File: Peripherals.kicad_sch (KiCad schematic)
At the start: 26 parts, among them J2 Conn_01x02, M1 Vibrator DC Motor, U1 MAX30102, U10 DRV2603RUNR, U2 BMI270, U3 OPT3004DNPR, U4 LPS22DF, U5 W25Q32JVSS

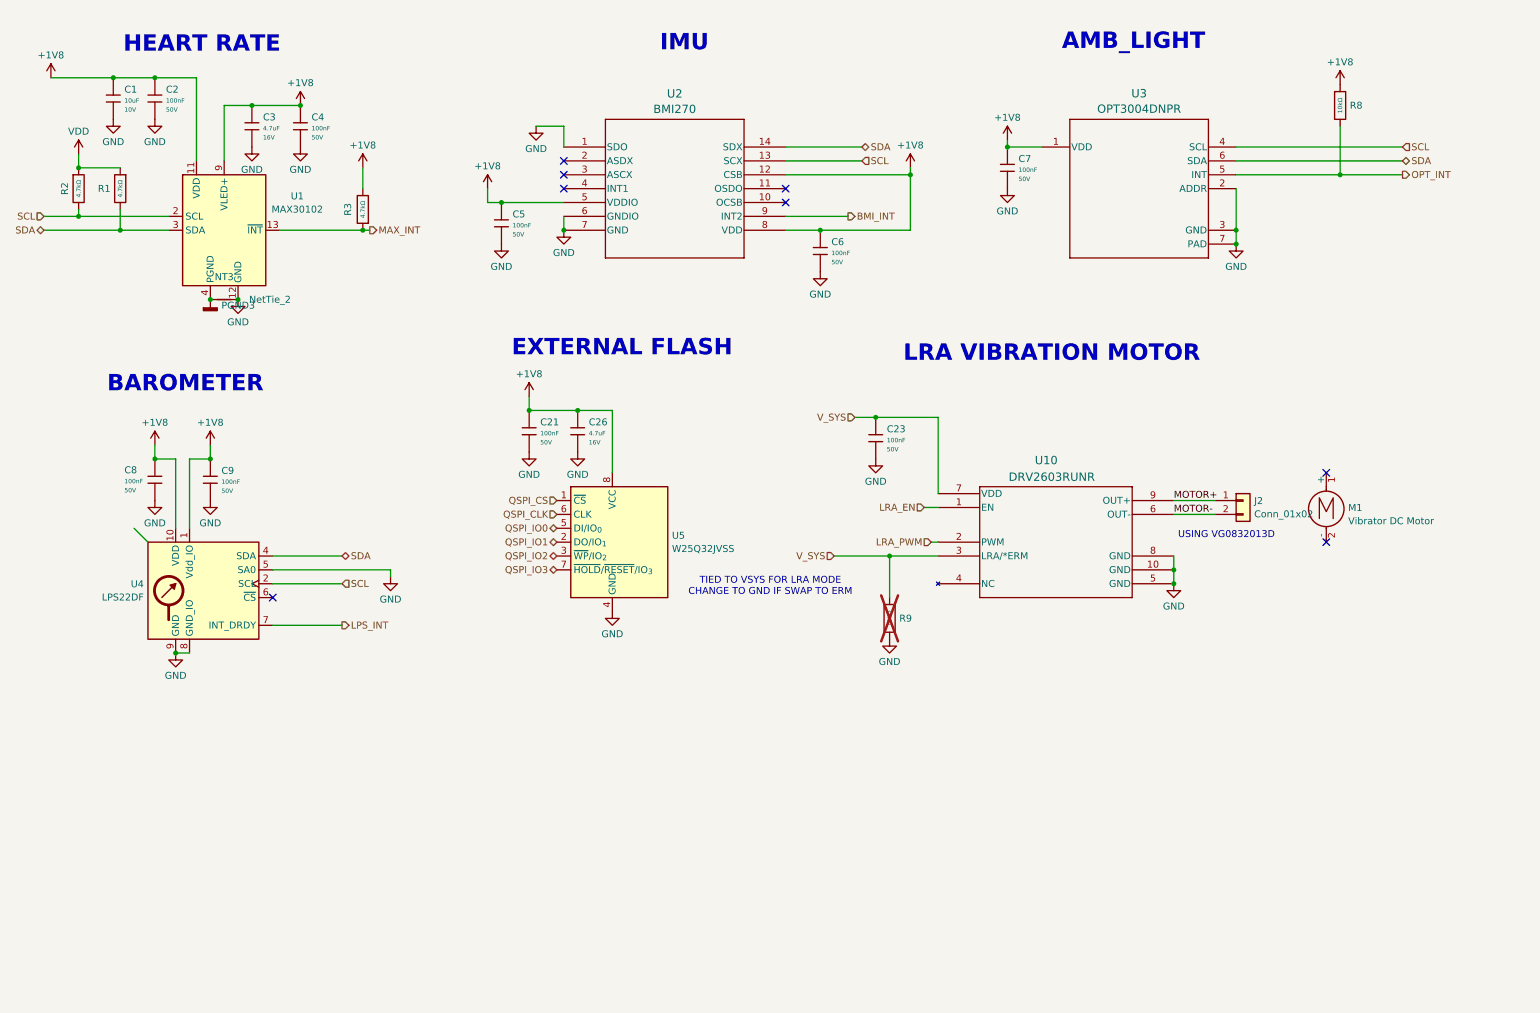
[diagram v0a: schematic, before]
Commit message: Update most sym/footprint libraries
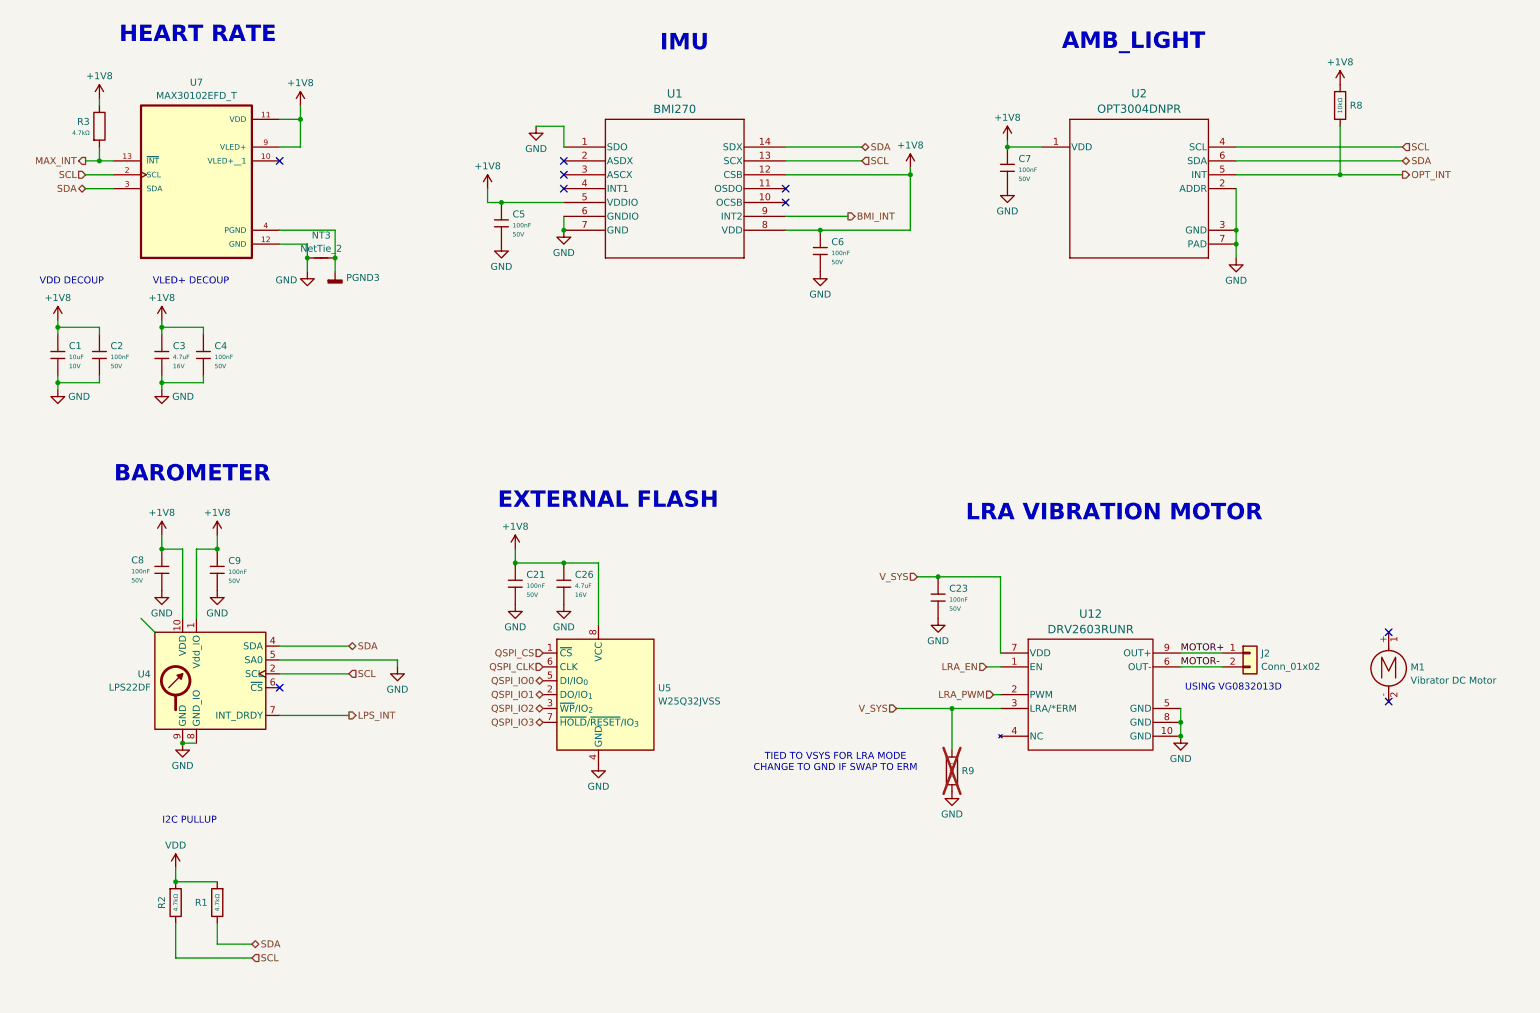
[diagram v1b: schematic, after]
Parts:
- removed U1: MAX30102, OptoDevice:Maxim_OLGA-14_3.3x5.6mm_P0.8mm, symbol Sensor:MAX30102
- removed U10: DRV2603RUNR, DRV:RUN10_TEX, symbol 2026-04-14_20-16-38:DRV2603RUNR
- removed U2: BMI270, BMI:BMI270_BOS, symbol 2026-04-08_00-20-06:BMI270
- removed U3: OPT3004DNPR, OPT:DNP0006A, symbol 2026-04-08_01-09-15:OPT3004DNPR
- added U1: BMI270, Smart_Watch:BMI270_BOS-L, symbol Smart_Watch:BMI270
- added U12: DRV2603RUNR, Smart_Watch:RUN10_TEX, symbol Smart_Watch:DRV2603RUNR
- added U2: OPT3004DNPR, Smart_Watch:DNP0006A, symbol Smart_Watch:OPT3004DNPR
- added U7: MAX30102EFD_T, Smart_Watch:XDCR_MAX30101EFD_, symbol Smart_Watch:MAX30102EFD_T
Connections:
- net +1V8: now also C1.2, C2.2, U1.12 (CSB), U1.5 (VDDIO), U1.8 (VDD), U2.1 (VDD), U7.11 (VDD), U7.9 (VLED+); no longer C1.1, C2.1
- net BMI_INT: now also U1.9 (INT2)
- net GND: now also C1.1, C2.1, NT3.1, U1.1 (SDO), U1.6 (GNDIO), U1.7 (GND), U12.10 (GND), U12.5 (GND), U12.8 (GND), U2.2 (ADDR), U2.3 (GND), U2.7 (PAD), U7.12 (GND); no longer C1.2, C2.2, NT3.2
- net LRA_EN: now also U12.1 (EN)
- net LRA_PWM: now also U12.2 (PWM)
- net MAX_INT: now also U7.13 (~{INT})
- net MOTOR+: now also U12.9 (OUT+)
- net MOTOR-: now also U12.6 (OUT-)
- net OPT_INT: now also U2.5 (INT)
- net PGND3: now also NT3.2, U7.4 (PGND); no longer NT3.1
- net SCL: now also U1.13 (SCX), U2.4 (SCL), U7.2 (SCL)
- net SDA: now also U1.14 (SDX), U2.6 (SDA), U7.3 (SDA)
- net V_SYS: now also U12.3 (LRA/*ERM), U12.7 (VDD)
- no-connect marks 8 -> 9
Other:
- note added: "I2C PULLUP"
- note added: "VDD DECOUP"
- note added: "VLED+ DECOUP"
- moved on the sheet: C1, C2, C21, C23, C26, C3, C4, C8, C9, J2, M1, NT3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

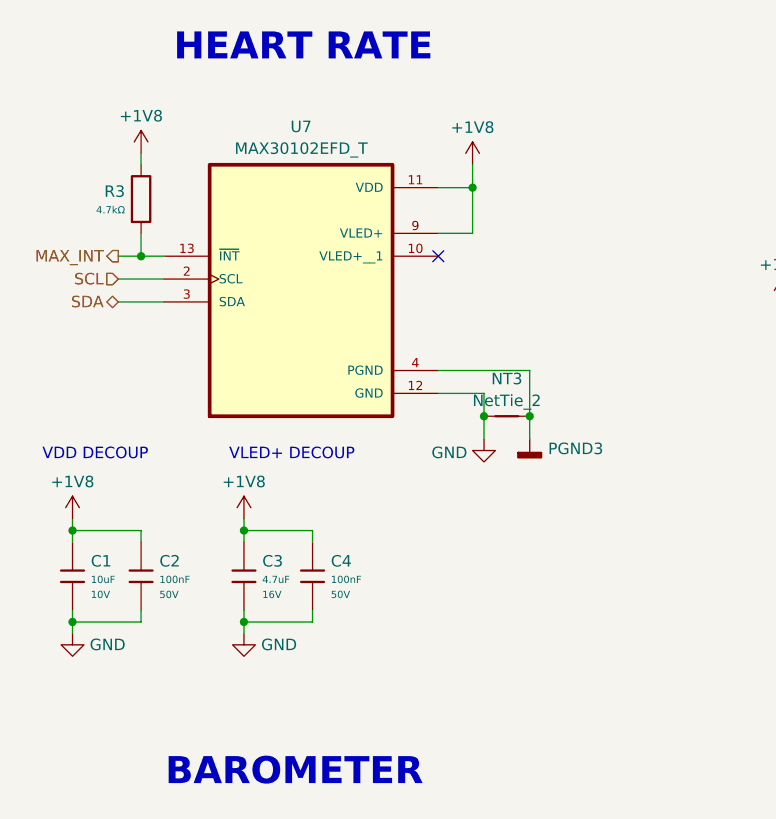
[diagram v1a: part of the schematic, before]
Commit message: Remove heart rate sensor from main board
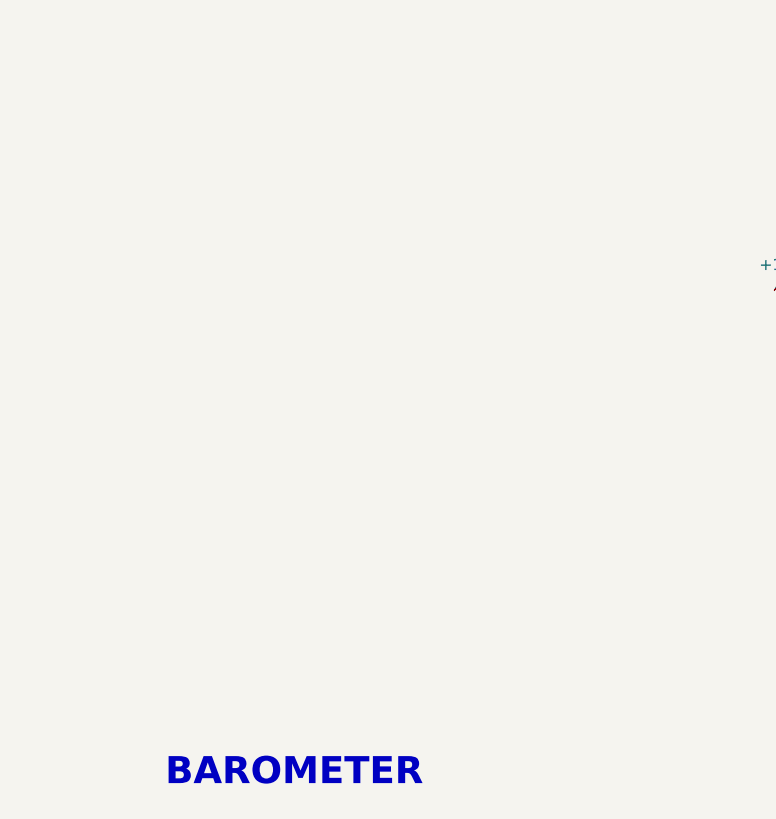
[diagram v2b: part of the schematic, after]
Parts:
- removed C1: 10uF, PCM_JLCPCB:C_0603, symbol PCM_JLCPCB-Capacitors:0603,10uF
- removed C2, C4: 100nF, PCM_JLCPCB:C_0603, symbol PCM_JLCPCB-Capacitors:0603,100nF
- removed C3: 4.7uF, PCM_JLCPCB:C_0603, symbol PCM_JLCPCB-Capacitors:0603,4.7uF
- removed NT3: NetTie_2, NetTie:NetTie-2_SMD_Pad0.5mm, symbol Device:NetTie_2
- removed R3: 4.7kΩ, PCM_JLCPCB:R_0603, symbol PCM_JLCPCB-Resistors:0603,4.7kΩ
- removed U7: MAX30102EFD_T, Smart_Watch:XDCR_MAX30101EFD_, symbol Smart_Watch:MAX30102EFD_T
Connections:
- no-connect marks 9 -> 8
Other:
- note removed: "HEART RATE"
- note removed: "VDD DECOUP"
- note removed: "VLED+ DECOUP"

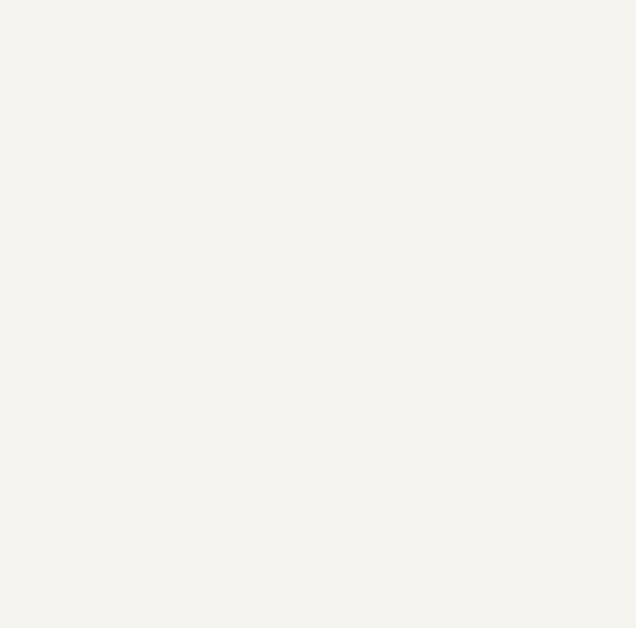
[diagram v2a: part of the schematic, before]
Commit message: Added Backpack Integration + Layout V1
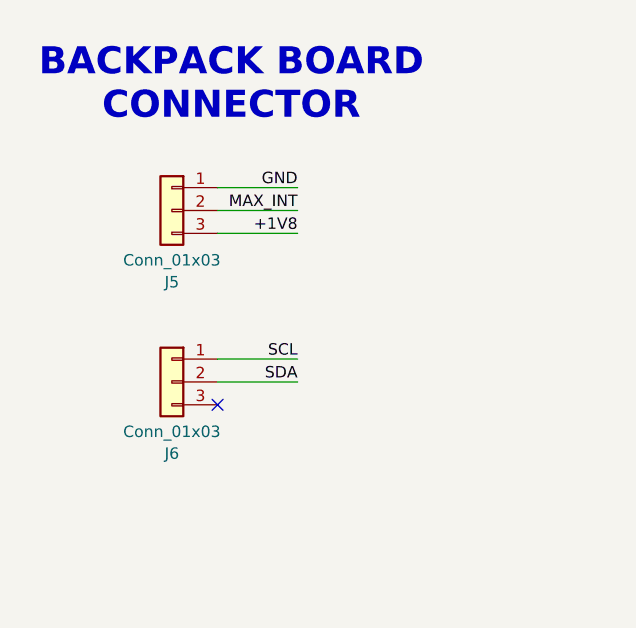
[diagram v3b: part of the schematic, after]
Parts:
- added J5, J6: Conn_01x03, Connector_PinHeader_1.27mm:PinHeader_1x03_P1.27mm_Vertical_SMD_Pin1Left, symbol Connector_Generic:Conn_01x03
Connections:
- net +1V8: now also J5.3 (Pin_3)
- net GND: now also J5.1 (Pin_1)
- net SCL: now also J6.1 (Pin_1)
- net SDA: now also J6.2 (Pin_2)
- new net MAX_INT: J5.2 (Pin_2)
- no-connect marks 8 -> 9
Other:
- note added: "BACKPACK BOARD CONNECTOR"

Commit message: Layout Midpoint, Updated Backpack Schem
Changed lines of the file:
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@@
 	(wire
 		(pts
-			(xy 52.07 55.88) (xy 43.18 55.88)
-		)
-		(stroke
-			(width 0)
-			(type default)
-		)
-	)
-	(wire
-		(pts
 			(xy 161.29 55.88) (xy 177.8 55.88)
 		)
@@
 	(wire
 		(pts
-			(xy 52.07 41.91) (xy 43.18 41.91)
+			(xy 43.18 41.91) (xy 60.96 41.91)
 		)
 		(stroke
@@
 	(wire
 		(pts
-			(xy 43.18 39.37) (xy 52.07 39.37)
-		)
-		(stroke
-			(width 0)
-			(type default)
-		)
-	)
-	(wire
-		(pts
-			(xy 52.07 58.42) (xy 43.18 58.42)
+			(xy 43.18 39.37) (xy 48.26 39.37)
 		)
 		(stroke
@@
 	(wire
 		(pts
+			(xy 52.07 34.29) (xy 57.15 34.29)
+		)
+		(stroke
+			(width 0)
+			(type default)
+		)
+	)
+	(wire
+		(pts
 			(xy 256.54 36.83) (xy 256.54 45.72)
 		)
@@
 	(wire
 		(pts
+			(xy 43.18 55.88) (xy 57.15 55.88)
+		)
+		(stroke
+			(width 0)
+			(type default)
+		)
+	)
+	(wire
+		(pts
 			(xy 50.8 182.88) (xy 50.8 186.69)
 		)
@@
 	(wire
 		(pts
+			(xy 43.18 58.42) (xy 57.15 58.42)
+		)
+		(stroke
+			(width 0)
+			(type default)
+		)
+	)
+	(wire
+		(pts
 			(xy 62.23 134.62) (xy 83.82 134.62)
 		)
@@
 	(wire
 		(pts
+			(xy 52.07 36.83) (xy 52.07 34.29)
+		)
+		(stroke
+			(width 0)
+			(type default)
+		)
+	)
+	(wire
+		(pts
 			(xy 227.33 146.05) (xy 227.33 148.59)
 		)
@@
 		)
 	)
-	(label "SCL"
-		(at 52.07 55.88 180)
-		(effects
-			(font
-				(size 1.27 1.27)
-			)
-			(justify right bottom)
-		)
-	)
-	(label "+1V8"
-		(at 52.07 41.91 180)
-		(effects
-			(font
-				(size 1.27 1.27)
-			)
-			(justify right bottom)
-		)
-	)
-	(label "GND"
-		(at 52.07 36.83 180)
-		(effects
-			(font
-				(size 1.27 1.27)
-			)
-			(justify right bottom)
-		)
-	)
-	(label "SDA"
-		(at 52.07 58.42 180)
-		(effects
-			(font
-				(size 1.27 1.27)
-			)
-			(justify right bottom)
-		)
-	)
-	(label "MAX_INT"
-		(at 52.07 39.37 180)
+	(hierarchical_label "MAX_INT"
+		(shape input)
+		(at 48.26 39.37 0)
 		(effects
 			(font
 				(size 1.27 1.27)
 			)
-			(justify right bottom)
+			(justify left)
 		)
 	)
@@
 		)
 	)
+	(hierarchical_label "SCL"
+		(shape input)
+		(at 57.15 55.88 0)
+		(effects
+			(font
+				(size 1.27 1.27)
+			)
+			(justify left)
+		)
+	)
 	(hierarchical_label "SDA"
 		(shape bidirectional)
@@
 		)
 	)
+	(hierarchical_label "SDA"
+		(shape bidirectional)
+		(at 57.15 58.42 0)
+		(effects
+			(font
+				(size 1.27 1.27)
+			)
+			(justify left)
+		)
+	)
 	(hierarchical_label "QSPI_IO0"
 		(shape bidirectional)
@@
 	)
 	(symbol
+		(lib_id "power:VDD")
+		(at 60.96 41.91 0)
+		(unit 1)
+		(body_style 1)
+		(exclude_from_sim no)
+		(in_bom yes)
+		(on_board yes)
+		(in_pos_files yes)
+		(dnp no)
+		(fields_autoplaced yes)
+		(property "Reference" "#PWR033"
+			(at 60.96 45.72 0)
+			(hide yes)
+			(show_name no)
+			(do_not_autoplace no)
+			(effects
+				(font
+					(size 1.27 1.27)
+				)
+			)
+		)
+		(property "Value" "+1V8"
+			(at 60.96 37.7769 0)
+			(show_name no)
+			(do_not_autoplace no)
+			(effects
+				(font
+					(size 1.27 1.27)
+				)
+			)
+		)
+		(property "Footprint" ""
+			(at 60.96 41.91 0)
+			(hide yes)
+			(show_name no)
+			(do_not_autoplace no)
+			(effects
+				(font
+					(size 1.27 1.27)
+				)
+			)
+		)
+		(property "Datasheet" ""
+			(at 60.96 41.91 0)
+			(hide yes)
+			(show_name no)
+			(do_not_autoplace no)
+			(effects
+				(font
+					(size 1.27 1.27)
+				)
+			)
+		)
+		(property "Description" "Power symbol creates a global label with name \"VDD\""
+			(at 60.96 41.91 0)
+			(hide yes)
+			(show_name no)
+			(do_not_autoplace no)
+			(effects
+				(font
+					(size 1.27 1.27)
+				)
+			)
+		)
+		(pin "1"
+		)
+		(instances
+			(project "Smart_Watch"
+				(path "/69095a4d-0a57-4fa3-aecb-1cfd89eedc11/bed567dd-6d09-419a-b99a-3e57c9439bd4/21b6cdb5-38b5-44be-b4b2-bd0733b126a2"
+					(reference "#PWR033")
+					(unit 1)
+				)
+			)
+		)
+	)
+	(symbol
 		(lib_id "PCM_JLCPCB-Capacitors:0603,100nF")
 		(at 161.29 59.69 0)
@@
 				)
 			)
+		)
+	)
+	(symbol
+		(lib_id "power:GND")
+		(at 57.15 34.29 0)
+		(unit 1)
+		(body_style 1)
+		(exclude_from_sim no)
+		(in_bom yes)
+		(on_board yes)
+		(in_pos_files yes)
+		(dnp no)
+		(fields_autoplaced yes)
+		(property "Reference" "#PWR09"
+			(at 57.15 40.64 0)
+			(hide yes)
+			(show_name no)
+			(do_not_autoplace no)
+			(effects
+				(font
+					(size 1.27 1.27)
+				)
+			)
+		)
+		(property "Value" "GND"
+			(at 59.055 35.56 0)
+			(show_name no)
+			(do_not_autoplace no)
+			(effects
+				(font
+					(size 1.27 1.27)
+				)
+				(justify left)
+			)
+		)
+		(property "Footprint" ""
+			(at 57.15 34.29 0)
+			(hide yes)
+			(show_name no)
+			(do_not_autoplace no)
+			(effects
+				(font
+					(size 1.27 1.27)
+				)
+			)
+		)
+		(property "Datasheet" ""
+			(at 57.15 34.29 0)
+			(hide yes)
+			(show_name no)
+			(do_not_autoplace no)
+			(effects
+				(font
+					(size 1.27 1.27)
+				)
+			)
+		)
+		(property "Description" "Power symbol creates a global label with name \"GND\" , ground"
+			(at 57.15 34.29 0)
+			(hide yes)
+			(show_name no)
+			(do_not_autoplace no)
+			(effects
+				(font
+					(size 1.27 1.27)
+				)
+			)
+		)
+		(pin "1"
+		)
+		(instances
+			(project "Smart_Watch"
+				(path "/69095a4d-0a57-4fa3-aecb-1cfd89eedc11/bed567dd-6d09-419a-b99a-3e57c9439bd4/21b6cdb5-38b5-44be-b4b2-bd0733b126a2"
+					(reference "#PWR09")
+					(unit 1)
+				)
+			)
